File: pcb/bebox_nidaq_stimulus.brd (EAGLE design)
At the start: 55.7 x 20.7 mm, 4 parts, among them J1 SJ-435107RS, J6 SJ-435107RS, U1 MCP23008-E/P, X1 71430-0101

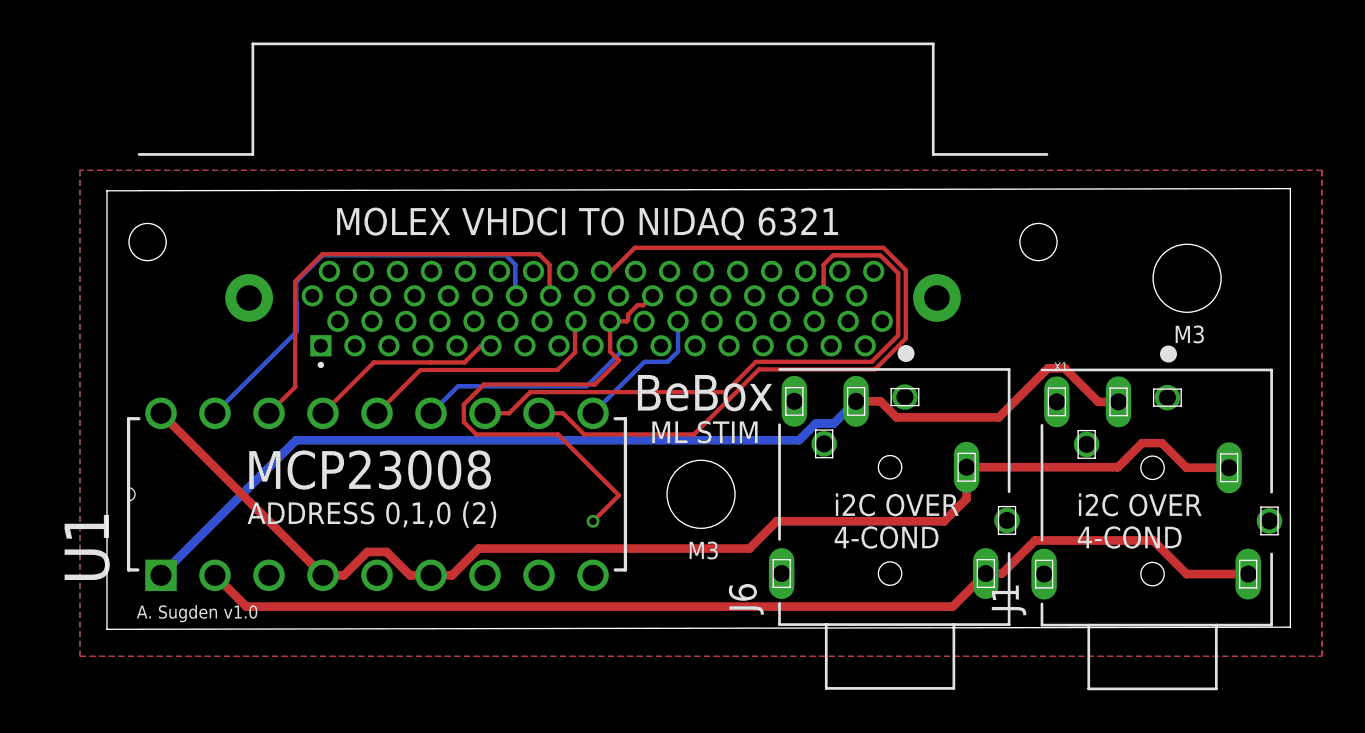
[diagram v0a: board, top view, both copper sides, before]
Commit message: Reorderd pins so that they would be more general across users.
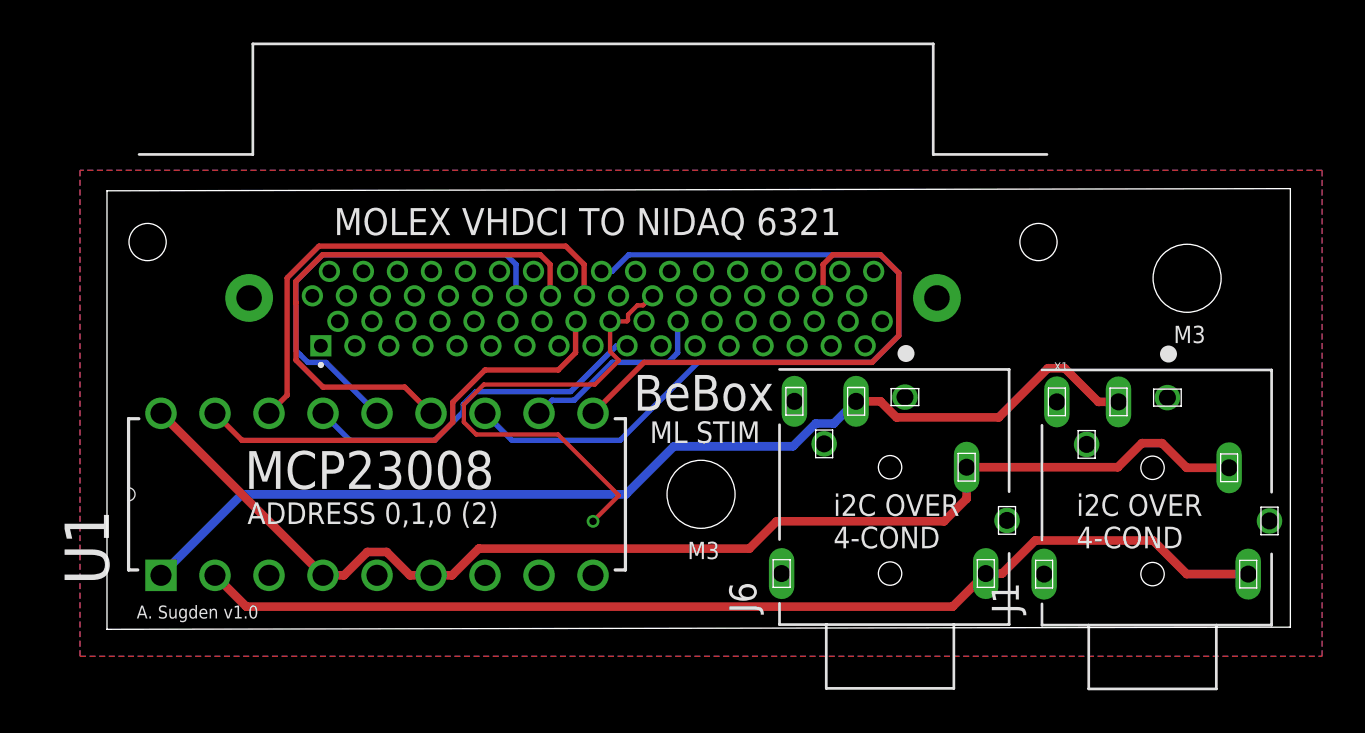
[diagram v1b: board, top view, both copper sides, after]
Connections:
- removed net P1.0: U1.15, X1.11
- new net P0.5: U1.16, X1.51
- net AI_2: now also U1.10; no longer U1.12
- net AO_0: now also U1.11; no longer U1.10
- net P0.0: now also U1.12; no longer U1.11
- net P0.2: now also U1.13; no longer U1.16
- net P0.3: now also U1.14; no longer U1.17
- net P0.4: now also U1.15; no longer U1.13
- net P0.6: now also U1.17; no longer U1.14
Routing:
- net P0.5: track 0.00 -> 23.1 mm
- net P0.6: track 12.0 -> 21.2 mm
- net P1.0: track 9.22 -> 0.00 mm
- net P0.4: track 10.5 -> 16.9 mm
- net AI_2: track 29.4 -> 24.4 mm
- net P0.2: track 20.9 -> 25.2 mm
- net AO_0: track 6.62 -> 9.18 mm
- net P0.0: track 38.0 -> 39.6 mm
- net P0.3: track 21.8 -> 20.8 mm
